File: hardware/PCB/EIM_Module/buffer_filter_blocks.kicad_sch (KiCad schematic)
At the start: 35 parts, among them U3 AD8014ARZ

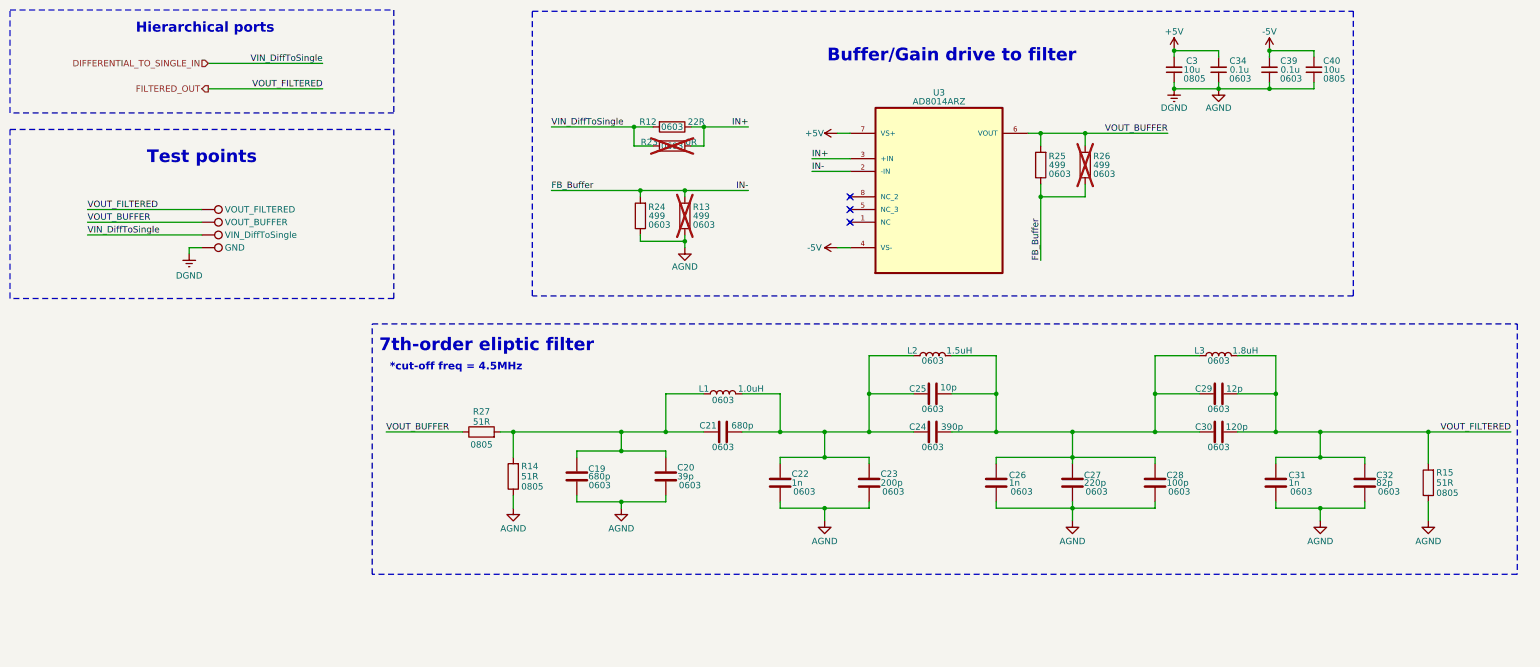
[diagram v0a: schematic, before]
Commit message: MAMS-33 Updated simulation final and update schematic and PCB
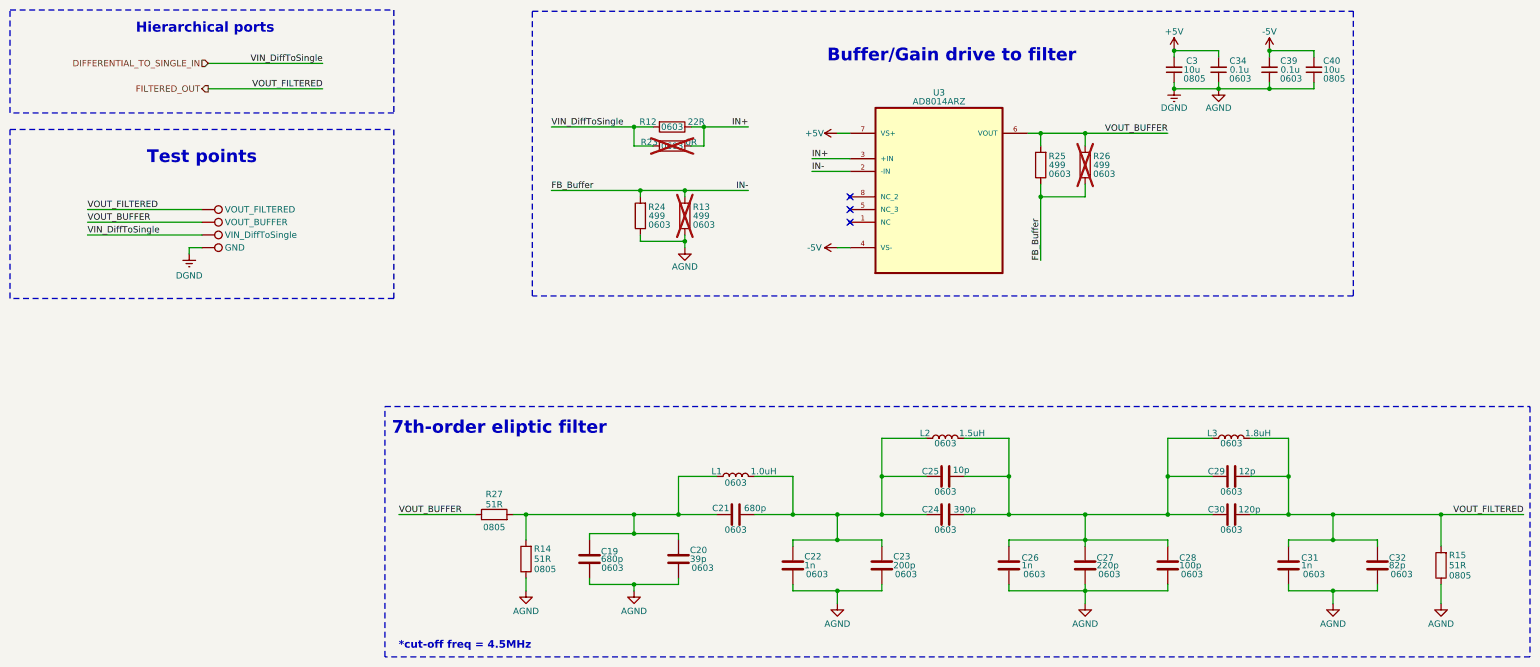
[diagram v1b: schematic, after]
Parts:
- C20, C24: SIze 0603 -> (none); Size (none) -> 0603
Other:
- moved on the sheet: C19, C20, C21, C22, C23, C24, C25, C26, C27, C28, C29, C30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

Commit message: MAMS-38 updated PCB layout for EIM with version using connector
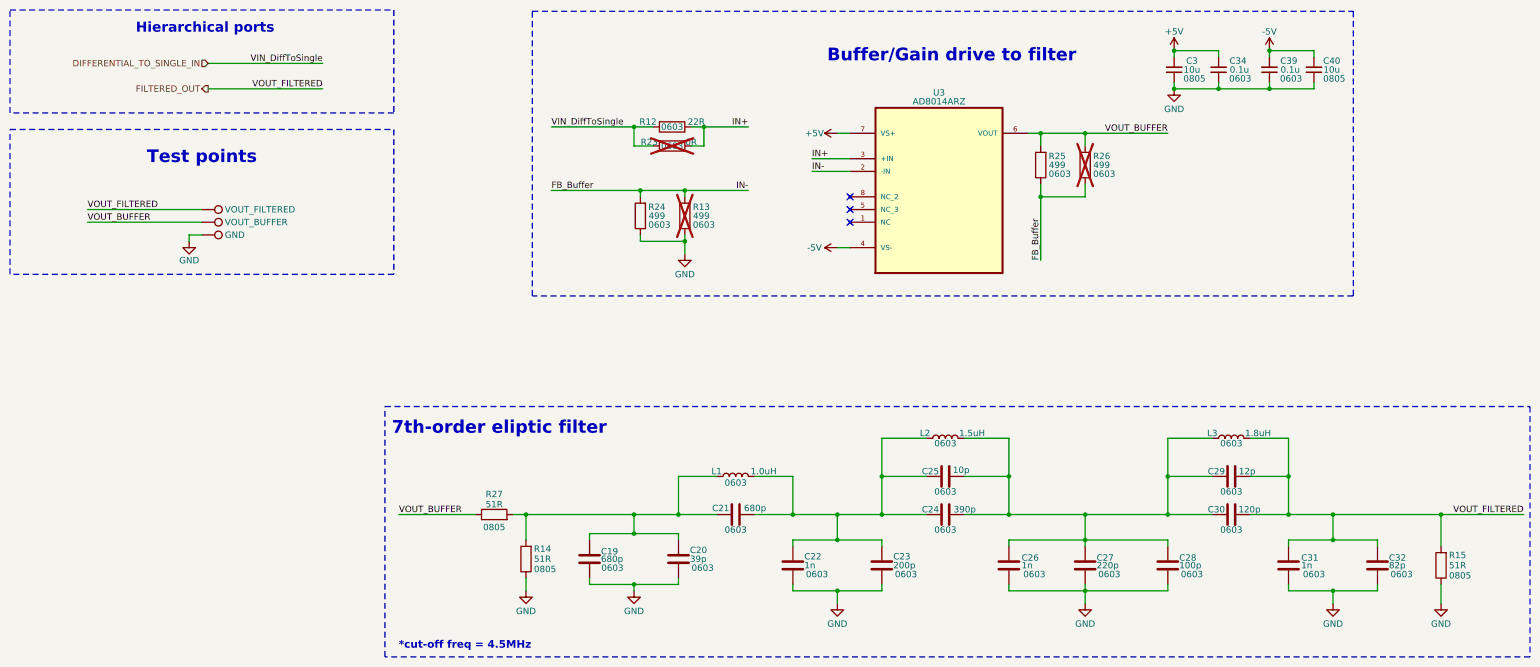
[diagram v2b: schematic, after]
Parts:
- removed TP24: VIN_DiffToSingle, TestPoint:TestPoint_Pad_D1.0mm, symbol Connector:TestPoint
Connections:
- net AGND renamed GND

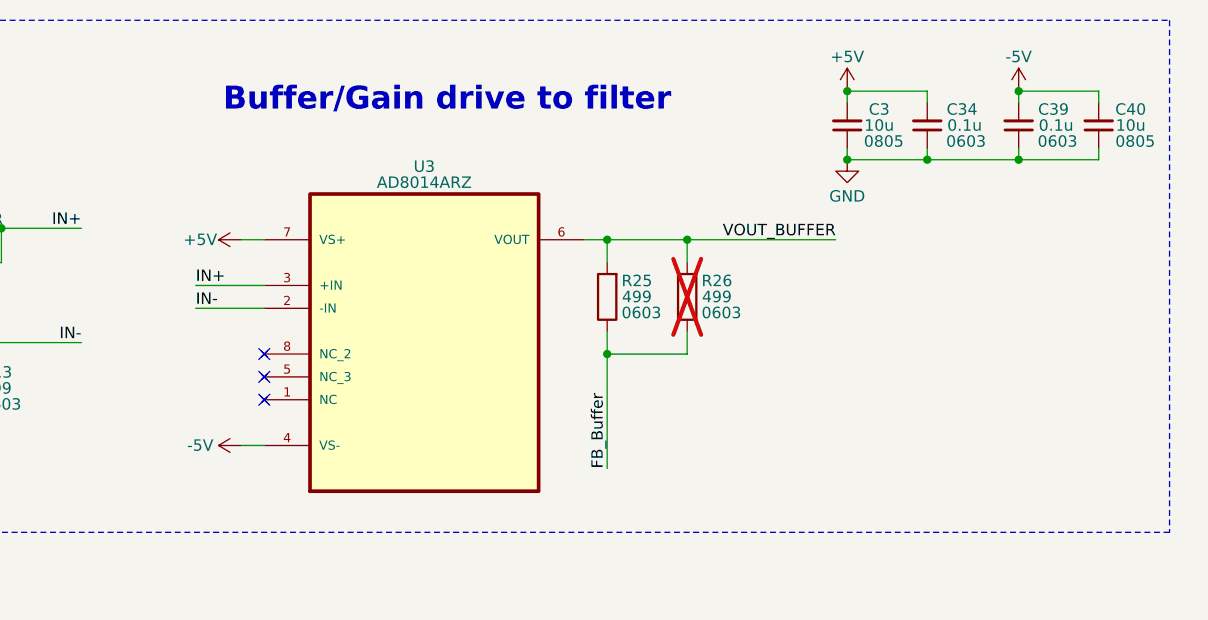
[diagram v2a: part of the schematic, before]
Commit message: MAMS-40 Updated PCB upto LPF
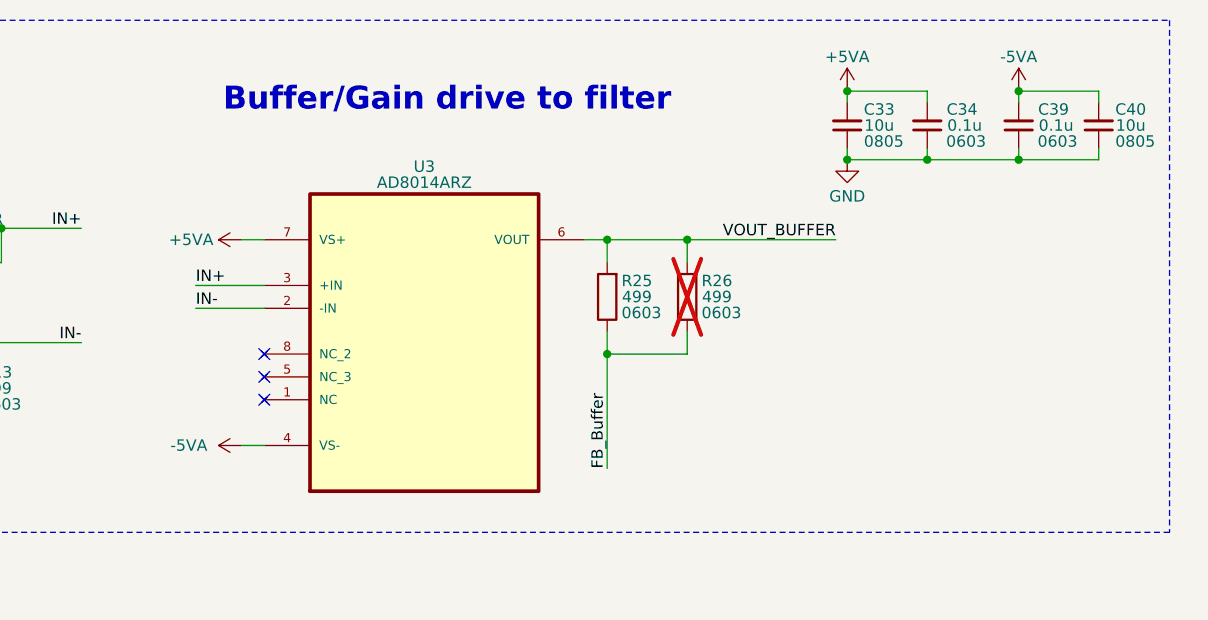
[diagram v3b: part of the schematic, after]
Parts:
- renumbered C3 to C33
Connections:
- net +5V renamed +5VA
- net -5V renamed -5VA
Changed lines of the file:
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@@
 			)
 		)
-		(property "Value" "+5V"
+		(property "Value" "+5VA"
 			(at 260.35 73.66 0)
 			(effects
@@
 			)
 		)
-		(property "Value" "-5V"
-			(at 188.468 116.84 90)
+		(property "Value" "-5VA"
+			(at 187.198 116.84 90)
 			(effects
 				(font
@@
 		(on_board yes)
 		(dnp no)
-		(property "Reference" "C3"
+		(property "Reference" "C33"
 			(at 263.906 79.502 0)
 			(effects
@@
 			(project "EIM_Module"
 				(path "/b637c68f-0528-4d93-9932-d8222f5b2863/cc414588-e43b-4dc6-856d-f34f45926a37"
-					(reference "C3")
+					(reference "C33")
 					(unit 1)
 				)
@@
 			)
 		)
-		(property "Value" "-5V"
+		(property "Value" "-5VA"
 			(at 279.4 73.66 0)
 			(effects
@@
 			)
 		)
-		(property "Value" "+5V"
-			(at 188.468 93.98 90)
-			(effects
-				(font
+		(property "Value" "+5VA"
+			(at 187.452 93.98 90)
+			(effects
+				(font
